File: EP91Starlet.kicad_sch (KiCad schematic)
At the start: 5 parts, among them M1 Module-mega-mcu144-0.7, M2 Module-wbo-0.5, M3 Module-knock-0.2, M4 Module-vr-max9924-0.1

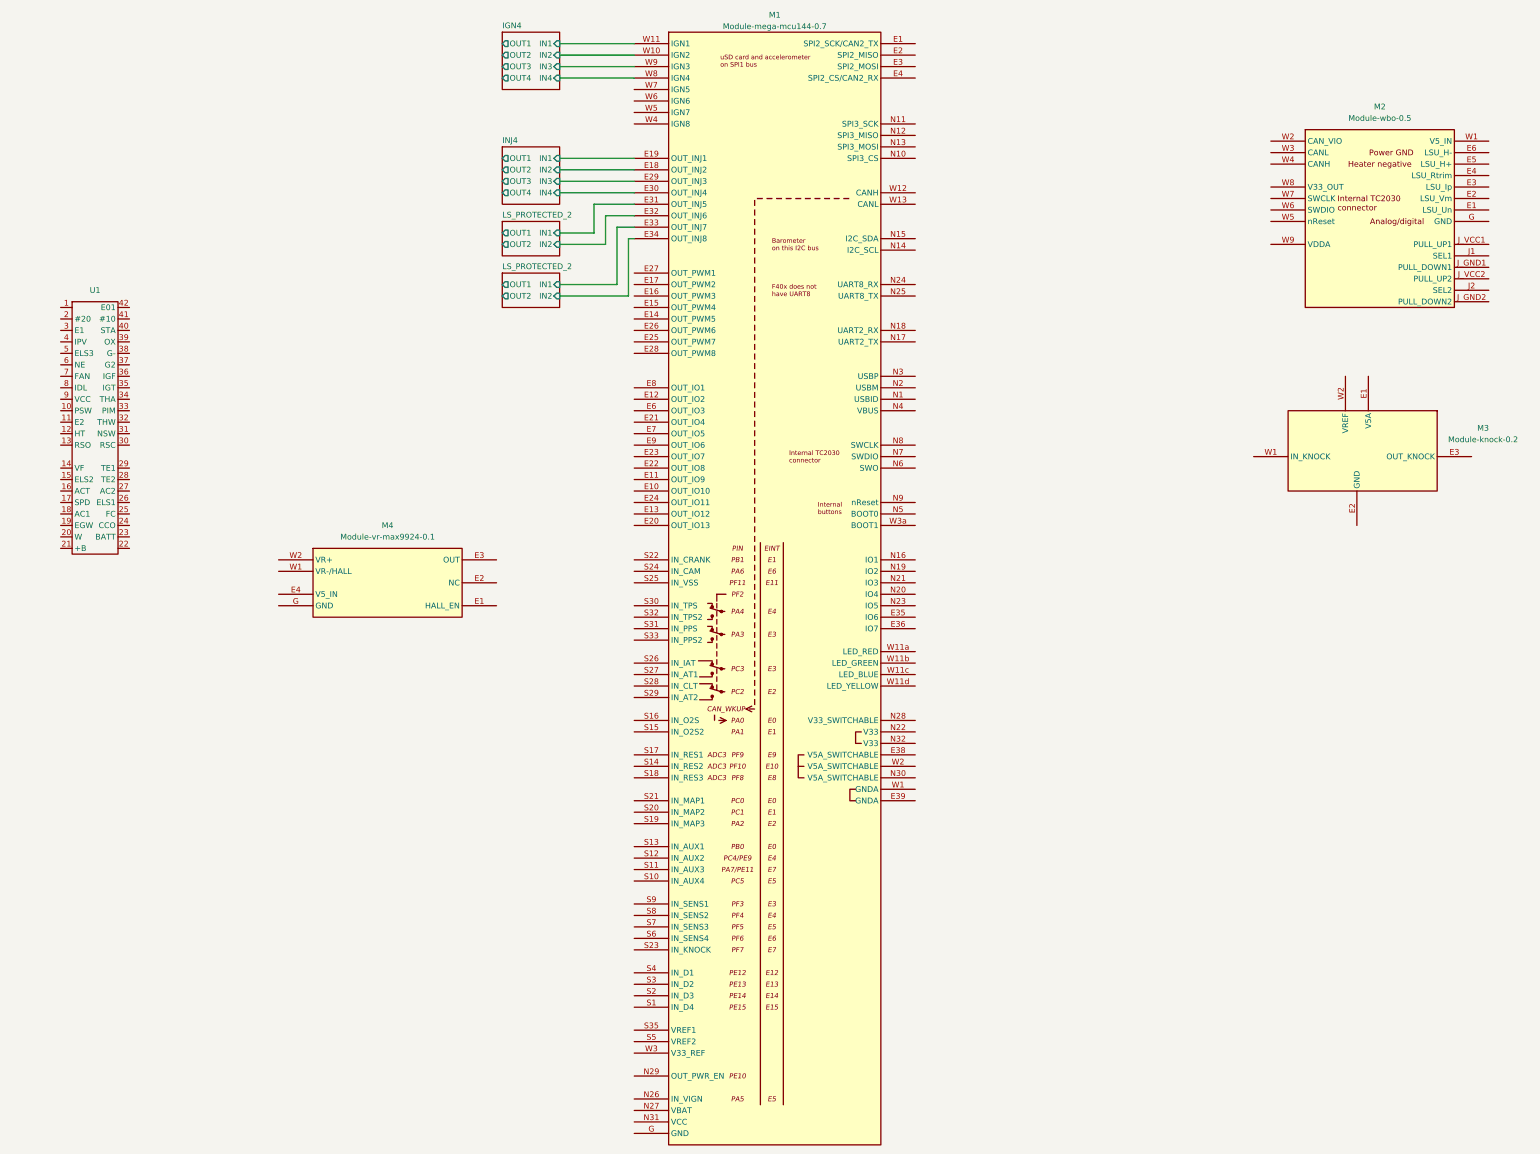
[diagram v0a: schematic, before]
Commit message: add submodules for ign and inj + flyback protected output
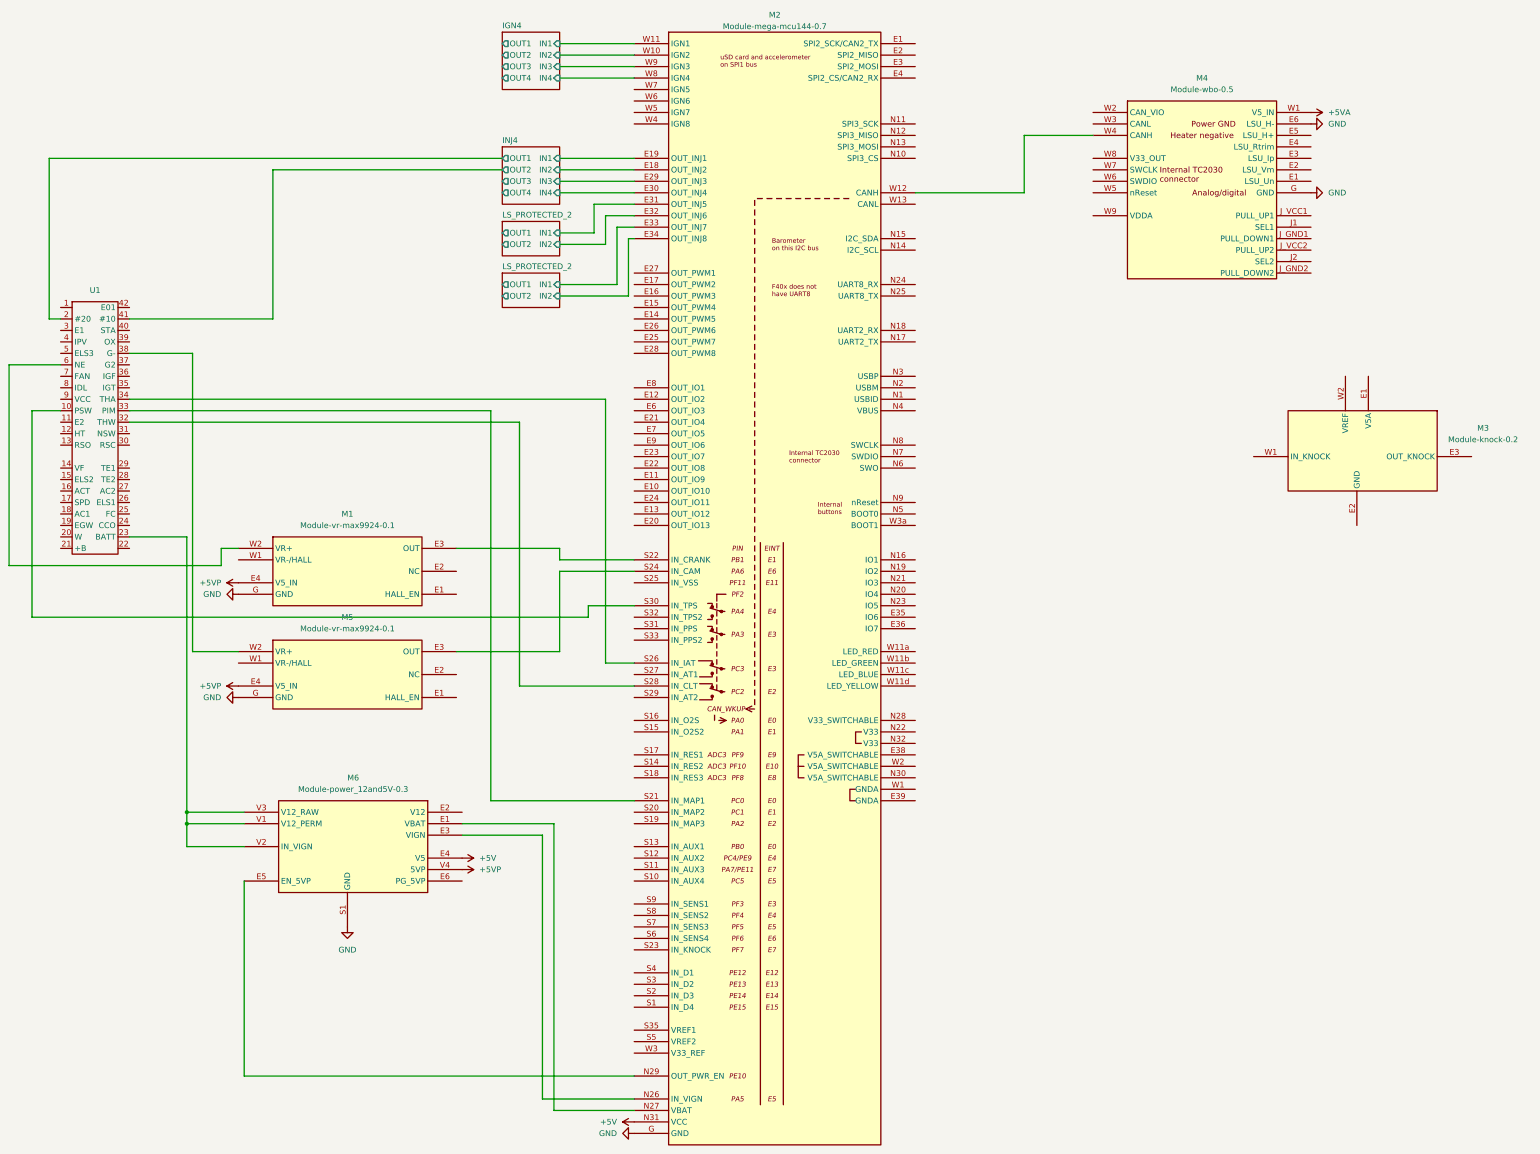
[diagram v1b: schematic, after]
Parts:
- removed M4: Module-vr-max9924-0.1, hellen-one-vr-max9924-0.1:vr-max9924, symbol vr-max9924:Module-vr-max9924-0.1
- added M1, M5: Module-vr-max9924-0.1, hellen-one-vr-max9924-0.1:vr-max9924, symbol vr-max9924:Module-vr-max9924-0.1
- added M6: Module-power_12and5V-0.3, power12_5:power_12and5V, symbol power_12and5V:Module-power_12and5V-0.3
- M2: renamed from M1; footprint hellen-one-mega-mcu144-0.7:mega-mcu144 -> mega144:mega-mcu144
- M3: footprint hellen-one-knock-0.2:knock -> knock:knock
- M4: renamed from M2; footprint hellen-one-wbo-0.5:wbo -> wbo:wbo
- U1: footprint EP91Starlet:4EFE ECU Connector -> EP91 libraries:4EFE ECU Connector
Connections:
- net LS_PROTECTED_2/IN1 is gone; now on net LS_PROTECTED_2/IN1: M2.E33 (OUT_INJ7)
- net LS_PROTECTED_2/IN2 is gone; now on net LS_PROTECTED_2/IN2: M2.E34 (OUT_INJ8)
- net INJ4/OUT1: now also U1.2 (#20)
- net INJ4/OUT2: now also U1.41 (#10)
- net LS_PROTECTED_2/IN1: no longer M2.E31 (OUT_INJ5)
- net LS_PROTECTED_2/IN2: no longer M2.E32 (OUT_INJ6)
- net at U1.10 (PSW): now also M2.S30 (IN_TPS)
- net at U1.23 (BATT): now also M6.V1 (V12_PERM), M6.V2 (IN_VIGN), M6.V3 (V12_RAW)
- net at U1.32 (THW): now also M2.S28 (IN_CLT)
- net at U1.33 (PIM): now also M2.S21 (IN_MAP1)
- net at U1.34 (THA): now also M2.S26 (IN_IAT)
- net at U1.38 (G-): now also M5.W2 (VR+)
- net at U1.6 (NE): now also M1.W2 (VR+)
- net GND: now reaches M2.G (GND)
- net GND: now also M4.E6 (LSU_H-), M4.G (GND), M1.G (GND), M5.G (GND), M6.S1 (GND)
- net at M2.N26 (IN_VIGN): now also M6.E3 (VIGN)
- net at M2.N27 (VBAT): now also M6.E1 (VBAT)
- net at M2.N29 (OUT_PWR_EN): now also M6.E5 (EN_5VP)
- net +5V: now reaches M2.N31 (VCC)
- net +5V: now also M6.E4 (V5)
- net at M2.S22 (IN_CRANK): now also M1.E3 (OUT)
- net at M2.S24 (IN_CAM): now also M5.E3 (OUT)
- net at M2.W12 (CANH): now also M4.W4 (CANH)
- net +5VA: now reaches M4.W1 (V5_IN)
- new net +5VP: M1.E4 (V5_IN), M5.E4 (V5_IN), M6.V4 (5VP)
- new net LS_PROTECTED_2/IN1: M2.E31 (OUT_INJ5)
- new net LS_PROTECTED_2/IN2: M2.E32 (OUT_INJ6)
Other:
- moved on the sheet: M4
